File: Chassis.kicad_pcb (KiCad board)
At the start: 2 copper layers, 125.5 x 120 mm, 46 parts, among them IC1 RT6285GSP, IC2 LV2862YDDCR, J1 FR_JST, J10 BL_XT30, J11 Sabre Vertical Header 6, J2 FR_XT30, J3 BR_JST, J4 BR_XT30, J5 IN_JST, J6 IN_XT60, J7 FL_JST, J8 FL_XT30, J9 BL_JST

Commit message: Add random microfit connector
For data outputs
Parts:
- added J12: Conn_01x12, Robomaster_ICs:CON_430451212_MOL, F.Cu at (116.1, 131.2)
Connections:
- net /24V -> 19V Buck Convertor/5V renamed +5V
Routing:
- net /CAN+: track 301.3 -> 299.6 mm
- net /CAN-: track 288.1 -> 286.8 mm

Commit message: U
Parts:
- removed H1, H2, H3: MountingHole, MountingHole:MountingHole_3.2mm_M3
- moved L1 63.4 mm to (165.0, 74.0), turned to -90 degrees
- moved C2 63.1 mm to (167.1, 87.0)
- moved C1 63.1 mm to (167.2, 84.7)
- moved D1 62.9 mm to (166.0, 81.0), turned to 0 degrees
- moved R6 59.3 mm to (158.0, 88.1), turned to -90 degrees
- moved IC1 54.7 mm to (163.0, 93.0), turned to 90 degrees
- moved J10 53.9 mm to (141.8, 118.4)
- moved D3 53.8 mm to (158.0, 93.2), turned to 90 degrees
- moved R3 52.6 mm to (167.2, 95.1), turned to 90 degrees
- moved J9 52.4 mm to (155.4, 118.3)
- moved C4 51.2 mm to (163.0, 85.1)
- moved C5 51.2 mm to (163.0, 88.0)
- moved J8 46.6 mm to (142.5, 56.0)
- moved J7 46.3 mm to (152.5, 56.0)
- moved C3 46.1 mm to (160.5, 98.9), turned to 180 degrees
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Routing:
- net /CAN+: track 299.6 -> 0.00 mm, vias 5 -> 0
- net /CAN-: track 286.8 -> 0.00 mm
- net /V_{OUT}: track 33.4 -> 0.00 mm, vias 2 -> 0
- net +24V: track 28.5 -> 0.00 mm, vias 2 -> 0
- net +5V: track 24.6 -> 0.00 mm, vias 2 -> 0
- net /24V -> 19V Buck Convertor/SW_{19}: track 13.7 -> 0.00 mm
- net /24V -> 19V Buck Convertor/FB_{19}: track 11.2 -> 0.00 mm
- net /24V -> 19V Buck Convertor/FB_{5}: track 7.42 -> 0.00 mm
- net /24V -> 19V Buck Convertor/SW_{5}: track 6.08 -> 0.00 mm
- net /24V -> 19V Buck Convertor/BOOT_{19}: track 5.19 -> 0.00 mm
- net Net-(D3-A): track 3.29 -> 0.00 mm
- net Net-(D4-A): track 3.24 -> 0.00 mm
- net /24V -> 19V Buck Convertor/BOOT_{5}: track 3.13 -> 0.00 mm
- net GND: track 0.21 -> 0.00 mm, vias 26 -> 0
- removed copper zone on B.Cu, net +24V
- removed copper zone on F.Cu, net /24V -> 19V Buck Convertor/FB_{19}
- removed copper zone on F.Cu, net /24V -> 19V Buck Convertor/SW_{5}
- removed copper zone on F.Cu, net /V_{OUT}
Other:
- board size 125.5 x 120 mm -> 78.7 x 94.5 mm

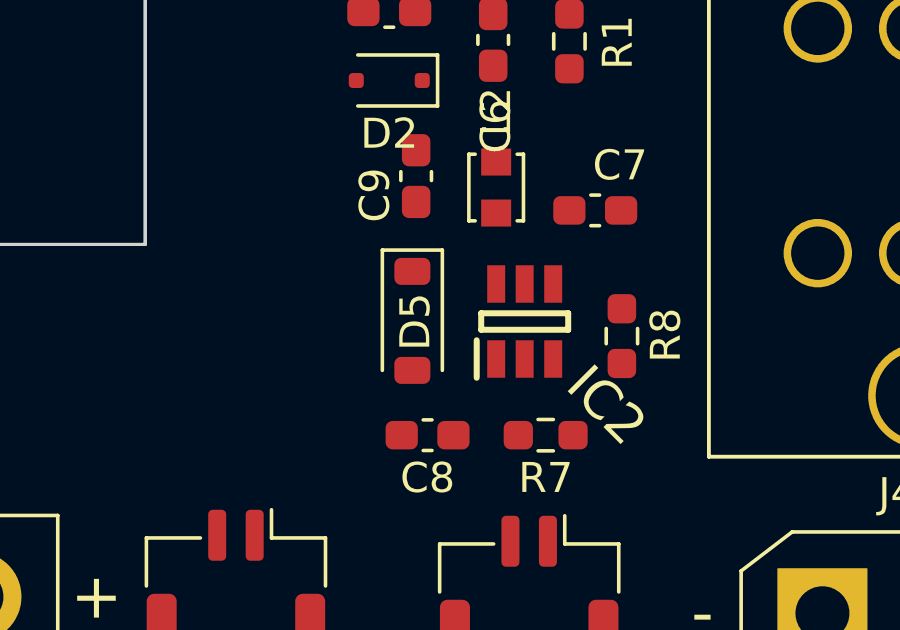
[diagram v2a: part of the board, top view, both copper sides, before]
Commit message: Delete buck folder
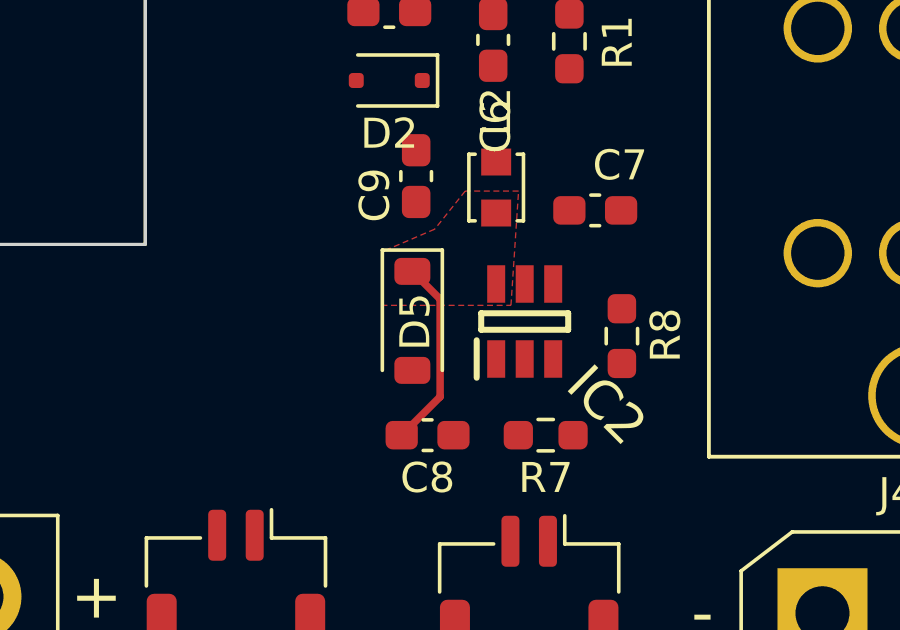
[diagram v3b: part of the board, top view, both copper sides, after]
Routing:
- net /24V -> 19V Buck Convertor/SW_{5}: track 0.00 -> 6.37 mm
- added copper zone on F.Cu, net /24V -> 19V Buck Convertor/SW_{5}
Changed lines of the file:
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@@
   (gr_rect (start 109.22 50.8) (end 109.22 73.66)
     (stroke (width 0.1) (type default)) (fill none) (layer "Edge.Cuts"))
-  (gr_rect (start 187.96 50.8) (end 109.22 50.8)
+  (gr_rect (start 109.22 50.8) (end 187.96 50.8)
     (stroke (width 0.1) (type default)) (fill none) (layer "Edge.Cuts"))
   (gr_rect (start 109.22 106.68) (end 152.4 106.68)
@@
     (style (thickness 0.15) (arrow_length 1.27) (text_position_mode 0) (extension_height 0.58642) (extension_offset 0.5) keep_text_aligned)
   )
+  (segment (start 161.304999 107.578999) (end 162.229999 108.503999) (width 0.25) (layer "F.Cu") (net 19))
+  (segment (start 162.229999 111.7595) (end 160.9505 113.038999) (width 0.25) (layer "F.Cu") (net 19))
+  (segment (start 162.229999 108.503999) (end 162.229999 111.7595) (width 0.25) (layer "F.Cu") (net 19))
   (zone (net 0) (net_name "") (layer "F.Cu") (name "A1") (hatch edge 0.5)
     (connect_pads yes (clearance 0))
@@
       )
     )
+  )
+  (zone (net 19) (net_name "/24V -> 19V Buck Convertor/SW_{5}") (layer "F.Cu") (name "help me") (hatch edge 0.5)
+    (priority 2)
+    (connect_pads yes (clearance 0.5))
+    (min_thickness 0.25) (filled_areas_thickness no)
+    (fill yes (thermal_gap 0.5) (thermal_bridge_width 0.5) (island_removal_mode 2) (island_area_min 10))
+    (polygon
+      (pts
+        (xy 164.592 108.712)
+        (xy 164.846 104.902)
+        (xy 163.068 104.902)
+        (xy 162.052 106.172)
+        (xy 160.274 106.934)
+        (xy 160.274 108.712)
+      )
+    )

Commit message: began adding traces :p
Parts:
- moved C1 5.72 mm to (167.5, 90.4)
- moved C2 5.72 mm to (167.5, 92.7)
- moved R3 0.77 mm to (166.9, 95.9)
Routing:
- net /CAN-: track 0.00 -> 87.8 mm
- net /CAN+: track 0.00 -> 82.7 mm
- net +24V: track 0.00 -> 6.20 mm
- net Net-(D4-A): track 0.00 -> 3.24 mm
- added copper zone on B.Cu, net +24V
- removed copper zone on B.Cu, net GND
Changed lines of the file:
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@@
   (net 32 "unconnected-(J12-Pin_12-Pad12)")
   (footprint "Capacitor_SMD:C_0603_1608Metric_Pad1.08x0.95mm_HandSolder" (layer "F.Cu")
-    (at 167.1375 87)
+    (at 167.4865 92.71)
     (descr "Capacitor SMD 0603 (1608 Metric), square (rectangular) end terminal, IPC_7351 nominal with elongated pad for handsoldering. (Body size source: IPC-SM-782 page 76, https://www.pcb-3d.com/wordpress/wp-content/uploads/ipc-sm-782a_amendment_1_and_2.pdf), generated with kicad-footprint-generator")
     (tags "capacitor handsolder")
@@
   )
   (footprint "Resistor_SMD:R_0603_1608Metric_Pad0.98x0.95mm_HandSolder" (layer "F.Cu")
-    (at 167.165 95.1455 90)
+    (at 166.878 95.8615 90)
     (descr "Resistor SMD 0603 (1608 Metric), square (rectangular) end terminal, IPC_7351 nominal with elongated pad for handsoldering. (Body size source: IPC-SM-782 page 72, https://www.pcb-3d.com/wordpress/wp-content/uploads/ipc-sm-782a_amendment_1_and_2.pdf), generated with kicad-footprint-generator")
     (tags "resistor handsolder")
@@
   )
   (footprint "Capacitor_SMD:C_0603_1608Metric_Pad1.08x0.95mm_HandSolder" (layer "F.Cu")
-    (at 167.18102 84.678851)
+    (at 167.53002 90.388851)
     (descr "Capacitor SMD 0603 (1608 Metric), square (rectangular) end terminal, IPC_7351 nominal with elongated pad for handsoldering. (Body size source: IPC-SM-782 page 76, https://www.pcb-3d.com/wordpress/wp-content/uploads/ipc-sm-782a_amendment_1_and_2.pdf), generated with kicad-footprint-generator")
     (tags "capacitor handsolder")
@@
     (style (thickness 0.15) (arrow_length 1.27) (text_position_mode 0) (extension_height 0.58642) (extension_offset 0.5) keep_text_aligned)
   )
+  (segment (start 154.3 59.125) (end 163.096751 59.125) (width 0.25) (layer "F.Cu") (net 1))
+  (segment (start 154.8 116.103249) (end 155.703249 115.2) (width 0.25) (layer "F.Cu") (net 1))
+  (segment (start 157 69) (end 157.375 69.375) (width 0.25) (layer "F.Cu") (net 1))
+  (segment (start 157.375 69.375) (end 157.375 72.05) (width 0.25) (layer "F.Cu") (net 1))
+  (segment (start 154.8 116.375) (end 154.8 116.103249) (width 0.25) (layer "F.Cu") (net 1))
+  (segment (start 157.375 82.117173) (end 154.8 84.692173) (width 0.25) (layer "F.Cu") (net 1))
+  (segment (start 163.096751 59.125) (end 164.1 58.121751) (width 0.25) (layer "F.Cu") (net 1))
+  (segment (start 163.2 115.2) (end 164.575 116.575) (width 0.25) (layer "F.Cu") (net 1))
+  (segment (start 153.125 57.95) (end 154.3 59.125) (width 0.25) (layer "F.Cu") (net 1))
+  (segment (start 157 61.825) (end 157 69) (width 0.25) (layer "F.Cu") (net 1))
+  (segment (start 157.375 72.05) (end 157.375 82.117173) (width 0.25) (layer "F.Cu") (net 1))
+  (segment (start 154.3 59.125) (end 157 61.825) (width 0.25) (layer "F.Cu") (net 1))
+  (segment (start 164.1 58.121751) (end 164.1 57.85) (width 0.25) (layer "F.Cu") (net 1))
+  (segment (start 154.8 84.692173) (end 154.8 116.375) (width 0.25) (layer "F.Cu") (net 1))
+  (segment (start 155.703249 115.2) (end 163.2 115.2) (width 0.25) (layer "F.Cu") (net 1))
+  (segment (start 151.875 57.95) (end 151.875 66.023) (width 0.25) (layer "F.Cu") (net 2))
+  (segment (start 155.75 69) (end 155.375 69.375) (width 0.25) (layer "F.Cu") (net 2))
+  (segment (start 151.875 57.678249) (end 152.778249 56.775) (width 0.25) (layer "F.Cu") (net 2))
+  (segment (start 156.05 116.646751) (end 156.05 116.375) (width 0.25) (layer "F.Cu") (net 2))
+  (segment (start 156.05 116.375) (end 157.425 117.75) (width 0.25) (layer "F.Cu") (net 2))
+  (segment (start 151.875 66.023) (end 154.852 69) (width 0.25) (layer "F.Cu") (net 2))
+  (segment (start 155.375 72.05) (end 154.175 73.25) (width 0.25) (layer "F.Cu") (net 2))
+  (segment (start 161.775 56.775) (end 162.85 57.85) (width 0.25) (layer "F.Cu") (net 2))
+  (segment (start 151.875 57.95) (end 151.875 57.678249) (width 0.25) (layer "F.Cu") (net 2))
+  (segment (start 154.505249 117.602) (end 155.094751 117.602) (width 0.25) (layer "F.Cu") (net 2))
+  (segment (start 155.094751 117.602) (end 156.05 116.646751) (width 0.25) (layer "F.Cu") (net 2))
+  (segment (start 154.175 73.25) (end 154.175 117.271751) (width 0.25) (layer "F.Cu") (net 2))
+  (segment (start 154.175 117.271751) (end 154.505249 117.602) (width 0.25) (layer "F.Cu") (net 2))
+  (segment (start 154.852 69) (end 155.75 69) (width 0.25) (layer "F.Cu") (net 2))
+  (segment (start 152.778249 56.775) (end 161.775 56.775) (width 0.25) (layer "F.Cu") (net 2))
+  (segment (start 164.921751 117.75) (end 165.825 116.846751) (width 0.25) (layer "F.Cu") (net 2))
+  (segment (start 155.375 69.375) (end 155.375 72.05) (width 0.25) (layer "F.Cu") (net 2))
+  (segment (start 157.425 117.75) (end 164.921751 117.75) (width 0.25) (layer "F.Cu") (net 2))
+  (segment (start 165.825 116.846751) (end 165.825 116.575) (width 0.25) (layer "F.Cu") (net 2))
+  (segment (start 126.45 55.878295) (end 126.45 61.75) (width 0.25) (layer "F.Cu") (net 3))
+  (segment (start 126.215131 55.643426) (end 126.45 55.878295) (width 0.25) (layer "F.Cu") (net 3))
+  (segment (start 121.148688 55.643426) (end 124.390131 55.643426) (width 0.25) (layer "F.Cu") (net 7))
   (segment (start 161.304999 107.578999) (end 162.229999 108.503999) (width 0.25) (layer "F.Cu") (net 19))
   (segment (start 162.229999 111.7595) (end 160.9505 113.038999) (width 0.25) (layer "F.Cu") (net 19))
@@
     )
   )
-  (zone (net 4) (net_name "GND") (layer "B.Cu") (hatch edge 0.5)
+  (zone (net 3) (net_name "+24V") (layer "B.Cu") (hatch edge 0.5)
     (priority 1)
     (connect_pads (clearance 0.5))

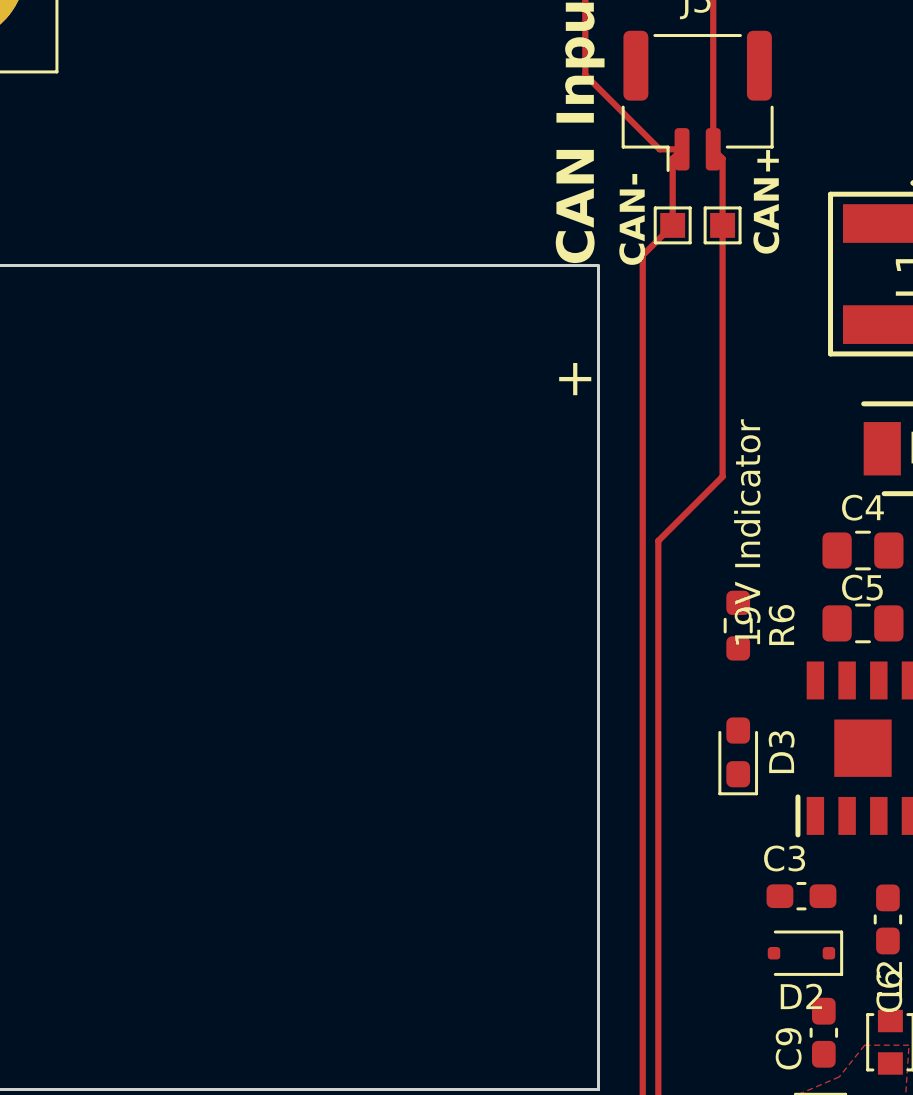
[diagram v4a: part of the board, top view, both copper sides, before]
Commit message: Added test points + part number for diode
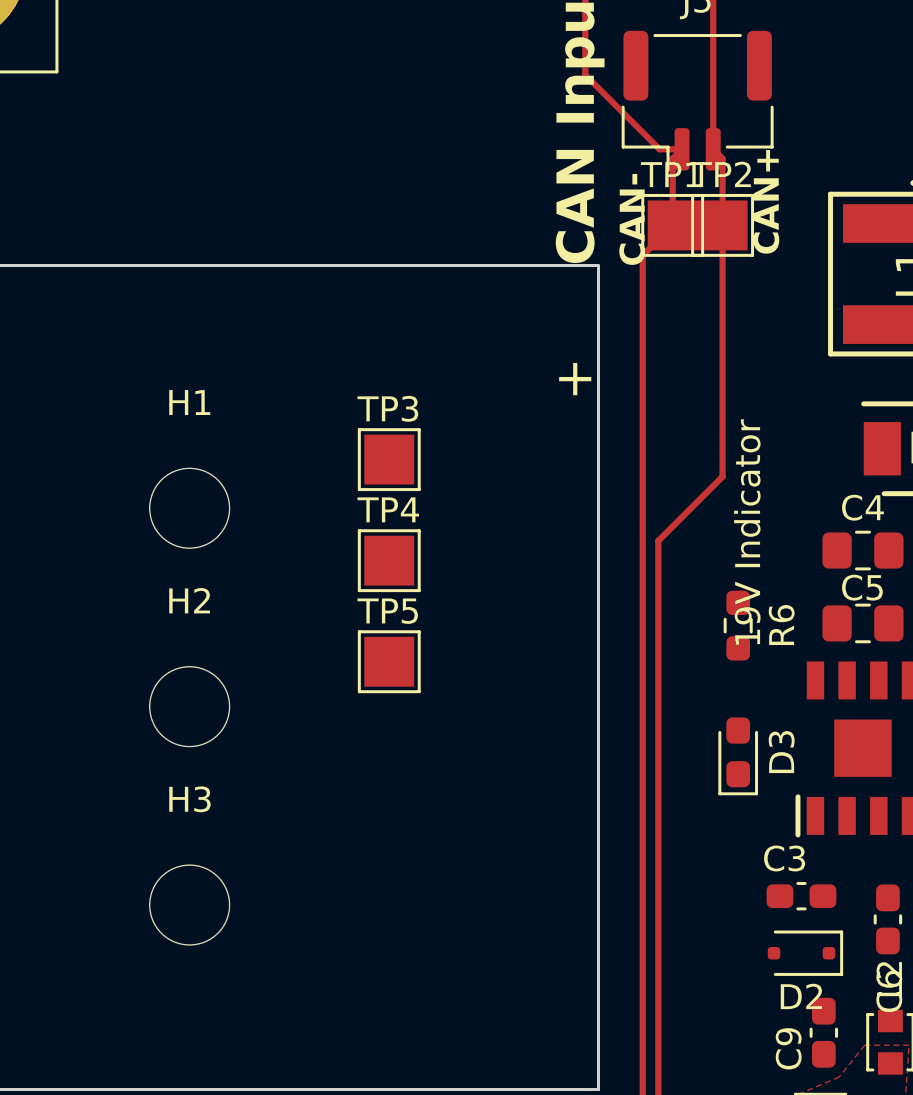
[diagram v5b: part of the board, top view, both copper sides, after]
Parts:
- added H1: MountingHole, MountingHole:MountingHole_3.2mm_M3, F.Cu at (136.0, 83.4)
- added H2: MountingHole, MountingHole:MountingHole_3.2mm_M3, F.Cu at (136.0, 91.3)
- added H3: MountingHole, MountingHole:MountingHole_3.2mm_M3, F.Cu at (136.0, 99.3)
- added TP3: TestPoint, TestPoint:TestPoint_Pad_2.0x2.0mm, F.Cu at (144.0, 81.4)
- added TP4: TestPoint, TestPoint:TestPoint_Pad_2.0x2.0mm, F.Cu at (144.0, 85.5)
- added TP5: TestPoint, TestPoint:TestPoint_Pad_2.0x2.0mm, F.Cu at (144.0, 89.5)
- D1: value B550 -> SR54F-AU_R2_000A1
- TP1, TP2: footprint TestPoint:TestPoint_Pad_1.0x1.0mm -> TestPoint:TestPoint_Pad_2.0x2.0mm
